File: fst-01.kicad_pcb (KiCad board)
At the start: 2 copper layers, 26.5 x 13.1 mm, 25 parts, among them J1 USB_A, K1 CONN_3, K2 CONN_2, K3 CONN_2, U1 STM32F103TB, U2 LP2985-33DBVR, U3 NUF2221W1, U4 SST25VF032B, X1 12MHz

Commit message: fst-01sz.
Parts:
- removed C10: 4.7uF, FST:c_0603
- removed C11: 0.1uF, FST:c_0402
- removed CE_mark: Symbol_CE_SilkScreen_5mm, Symbols:Symbol_CE_SilkScreen_5mm
- removed K2: CONN_2, SIL-2-0
- removed K3: CONN_2, SIL-2-2
- removed REF***: WEEE-Logo_4.2x6mm_SilkScreen, FST:WEEE-Logo_4.2x6mm_SilkScreen
- removed U4: SST25VF032B, WSON8
- added REF**: pad2, FST:pad1, F.Cu at (110.4, 93.6)
- added REF**: pad1, FST:pad1, F.Cu at (118.8, 94.2)
- C9: value 0.01uF -> 4.7uF; footprint FST:c_0402 -> FST:c_0603
- FST-LOGO: footprint FST-LOGO -> FST:FST-LOGO
- J1: footprint FST:USB-A-PLUG -> FST:USB-A-ZT01
- K1: footprint SIL-3-2 -> FST:SIL-5
- U2: value LP2985-33DBVR -> MCP1700-3302E; footprint FST:SOT23-5 -> Package_TO_SOT_SMD:SOT-23
- U3: footprint SOT363 -> FST:SOT363
- moved C2 15.0 mm to (123.5, 99.3), turned to 180 degrees
- moved X1 14.3 mm to (124.0, 101.9), turned to 90 degrees
- moved K1 13.4 mm to (112.8, 103.2)
- moved U3 11.9 mm to (112.8, 96.8), turned to 0 degrees
- moved D1 11.1 mm to (110.1, 99.0), turned to 270 degrees
- moved C1 11.0 mm to (121.8, 102.8), turned to 90 degrees
- moved C7 9.74 mm to (113.5, 100.8), turned to 90 degrees
- moved C8 9.69 mm to (121.6, 94.9), turned to 270 degrees
- moved C6 9.59 mm to (115.3, 94.5), turned to 0 degrees
- moved C4 8.92 mm to (121.8, 97.5), turned to 270 degrees
- moved C5 8.86 mm to (120.0, 102.5), turned to 180 degrees
- moved FST-LOGO 7.71 mm to (117.6, 98.6)
- moved R1 7.16 mm to (110.7, 101.5), turned to 180 degrees
- moved C3 6.86 mm to (117.7, 102.5), turned to 180 degrees
- moved C9 5.96 mm to (123.8, 94.2), turned to 0 degrees
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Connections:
- C9 pad 1: Net-(C9-Pad1) -> /VBUS
- D1 pad 1: GND -> Net-(D1-Pad1)
- D1 pad 2: Net-(D1-Pad2) -> /LED
- K1 pad 1: GND -> +3V3
- K1 pad 2: /SWCLK -> /SWDIO
- K1 pad 3: /SWDIO -> /SWCLK
- R1 pad 1: Net-(D1-Pad2) -> Net-(D1-Pad1)
- R1 pad 2: /LED -> GND
- U1 pad 10: /PA3 -> Net-(U1-Pad10)
- U1 pad 11: /NSS -> Net-(U1-Pad11)
- U1 pad 12: /CLK -> Net-(U1-Pad12)
- U1 pad 13: /MISO -> Net-(U1-Pad13)
- U1 pad 14: /MOSI -> Net-(U1-Pad14)
- U1 pad 15: /LED -> Net-(U1-Pad15)
- U1 pad 16: (no net) -> Net-(U1-Pad16)
- U1 pad 20: (no net) -> /LED
- U1 pad 21: (no net) -> Net-(U1-Pad21)
- U1 pad 22: (no net) -> Net-(U1-Pad22)
- U1 pad 29: (no net) -> Net-(U1-Pad29)
- U1 pad 30: (no net) -> Net-(U1-Pad30)
- U1 pad 31: (no net) -> Net-(U1-Pad31)
- U1 pad 32: (no net) -> Net-(U1-Pad32)
- U1 pad 33: (no net) -> Net-(U1-Pad33)
- U1 pad 34: (no net) -> Net-(U1-Pad34)
- U1 pad 7: (no net) -> Net-(U1-Pad7)
- U1 pad 8: (no net) -> Net-(U1-Pad8)
- U1 pad 9: /PA2 -> Net-(U1-Pad9)
- U2 pad 1: /VBUS -> GND
- U2 pad 2: GND -> +3V3
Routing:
- net +3V3: track 87.6 -> 53.1 mm, vias 6 -> 3
- net GND: track 94.2 -> 68.8 mm, vias 6 -> 2
- net /D-_PLUG: track 1.78 -> 18.2 mm, vias 0 -> 2
- net /MISO: track 12.7 -> 0.00 mm
- net /D+_PLUG: track 5.87 -> 17.8 mm, vias 0 -> 2
- net /NSS: track 10.5 -> 0.00 mm
- net /PA2: track 10.4 -> 0.00 mm
- net /NRST: track 2.17 -> 12.4 mm, vias 0 -> 2
- net /PA3: track 7.92 -> 0.00 mm
- net /MOSI: track 7.49 -> 0.00 mm
- net /VBUS: track 13.7 -> 6.37 mm
- net /CLK: track 5.52 -> 0.00 mm
- net Net-(U1-Pad10): track 0.00 -> 1.95 mm
- net /OSC_OUT: track 7.98 -> 6.38 mm
- net Net-(D1-Pad1): track 0.00 -> 1.41 mm
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- removed copper zone on F.Cu, net /VBUS
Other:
- board size 26.5 x 13.1 mm -> 20.8 x 12.2 mm
- rule pad_to_mask_clearance: 0.1524 -> 0.0762
- board text added: "FST-01SZ"
- board text removed: "FST-01G"

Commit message: More change.
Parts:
- removed the C4 at (121.8, 97.5)
- added C1: 0.1uF, FST:c_0402, F.Cu at (122.5, 97.5)
- moved C7 6.74 mm to (116.0, 94.5), turned to 0 degrees
- moved C6 6.33 mm to (114.3, 100.8), turned to 90 degrees
- moved C2 0.76 mm to (124.3, 99.3)
- moved C3 0.76 mm to (122.6, 102.8)
- moved C4 0.76 mm to (120.8, 102.5)
- moved C5 0.76 mm to (118.4, 102.5)
- moved C8 0.76 mm to (122.4, 94.9)
- moved C9 0.76 mm to (124.6, 94.2)
- moved K1 0.76 mm to (113.5, 103.2)
- moved REF** 0.76 mm to (119.6, 94.2)
- moved U1 0.76 mm to (118.3, 98.5)
- moved U2 0.76 mm to (125.1, 96.6)
- moved U3 0.76 mm to (113.6, 96.8)
- moved X1 0.76 mm to (124.8, 101.9)
- moved FST-LOGO 0.74 mm to (118.3, 98.7)
- renumbered C1 to C3, C5 to C4, C3 to C5
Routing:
- net GND: track 68.8 -> 77.4 mm
- net /VBUS: track 6.37 -> 4.36 mm
- net /D-_PLUG: track 18.2 -> 17.1 mm
- net /LED: track 5.85 -> 6.59 mm
- net +3V3: track 53.1 -> 52.5 mm
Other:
- board size 20.8 x 12.2 mm -> 21 x 12.6 mm
- net class Default: via_dia 0.8001 -> 0.8; via_drill 0.59944 -> 0.5
- net class GND: via_dia 0.8001 -> 0.8; via_drill 0.59944 -> 0.5
- net class VBUS: via_dia 0.8001 -> 0.8; via_drill 0.59944 -> 0.5
- net class VDD: via_dia 0.8001 -> 0.8; via_drill 0.59944 -> 0.5
- rule trace_min: 0.20066 -> 0.2
- rule via_min_drill: 0.50038 -> 0.5
- rule via_min_size: 0.8001 -> 0.8

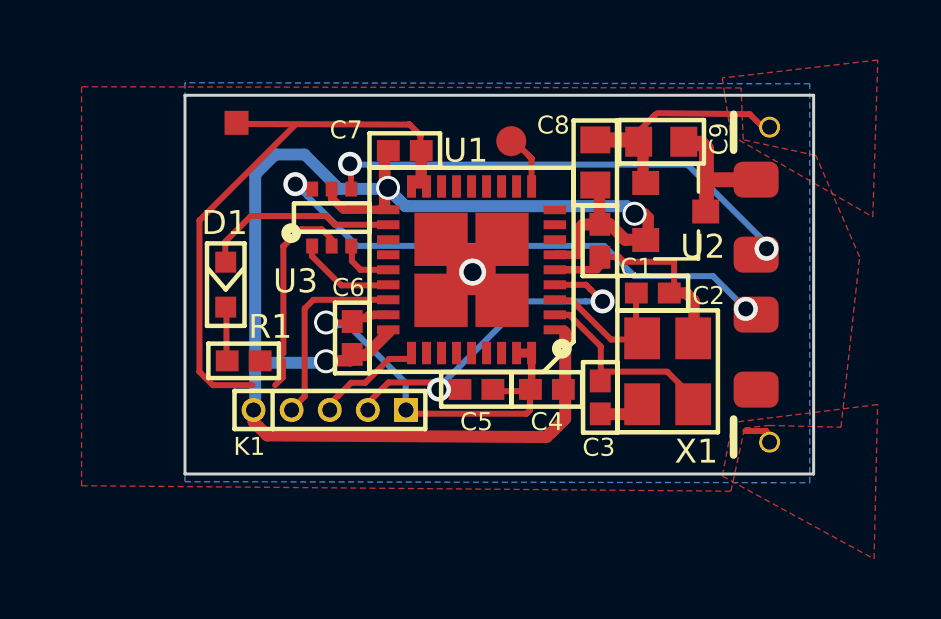
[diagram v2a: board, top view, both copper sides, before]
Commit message: Add hole sensor, drv5032.
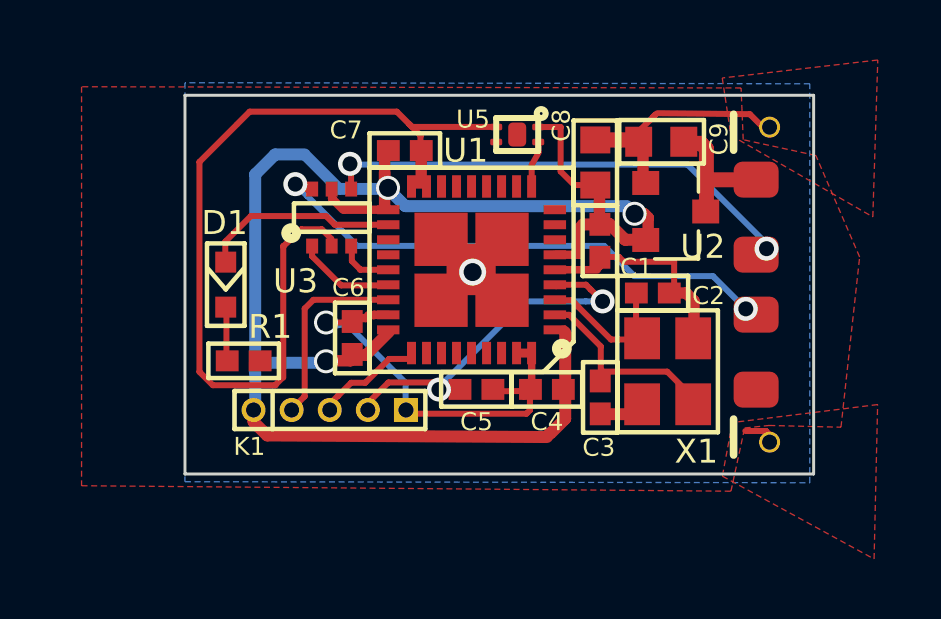
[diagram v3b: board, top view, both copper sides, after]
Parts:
- removed REF**: pad2, FST:pad1
- removed REF**: pad1, FST:pad1
- added U5: X2SON, FST:X2SON, F.Cu at (119.8, 94.0)
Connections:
- U1 pad 10: Net-(U1-Pad10) -> /PA3
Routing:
- net +3V3: track 52.5 -> 56.1 mm
- net GND: track 77.4 -> 80.8 mm
- net Net-(U1-Pad10): track 1.95 -> 0.00 mm
- net /PA3: track 0.00 -> 1.49 mm
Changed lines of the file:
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@@
     (thickness 1.6002)
     (drawings 6)
-    (tracks 258)
+    (tracks 263)
     (zones 0)
-    (modules 20)
+    (modules 19)
     (nets 33)
   )
@@
     (mod_text_size 1.524 1.524)
     (mod_text_width 0.3048)
-    (pad_size 1 1)
+    (pad_size 0.22 0.4)
     (pad_drill 0)
     (pad_to_mask_clearance 0.0762)
@@
   (net 30 "Net-(D1-Pad1)")
   (net 31 "Net-(U1-Pad14)")
-  (net 32 "Net-(U1-Pad10)")
+  (net 32 /PA3)
   (net_class Default "This is the default net class."
     (clearance 0.20066)
@@
     (add_net /OSC_IN)
     (add_net /OSC_OUT)
+    (add_net /PA3)
     (add_net /SWCLK)
     (add_net /SWDIO)
     (add_net /VBUS)
     (add_net "Net-(D1-Pad1)")
-    (add_net "Net-(U1-Pad10)")
     (add_net "Net-(U1-Pad11)")
     (add_net "Net-(U1-Pad12)")
@@
     (uvia_dia 0.50038)
     (uvia_drill 0.14986)
+  )
+  (module FST:X2SON (layer Front)
+    (at 119.7864 93.9927 270)
+    (fp_text reference U5 (at -0.508 1.4732 180) (layer F.SilkS)
+      (effects (font (size 0.6 0.6) (thickness 0.15)))
+    )
+    (fp_text value X2SON (at 0 -4.6 270) (layer F.Fab)
+      (effects (font (size 1 1) (thickness 0.15)))
+    )
+    (fp_circle (center -0.7 -0.8) (end -0.7 -0.7) (layer F.SilkS) (width 0.3))
+    (fp_line (start -0.55 -0.7) (end 0.55 -0.7) (layer F.SilkS) (width 0.2))
+    (fp_line (start 0.55 -0.7) (end 0.55 0.7) (layer F.SilkS) (width 0.2))
+    (fp_line (start 0.55 0.7) (end -0.55 0.7) (layer F.SilkS) (width 0.2))
+    (fp_line (start -0.55 0.7) (end -0.55 -0.7) (layer F.SilkS) (width 0.2))
+    (pad 5 smd roundrect (at 0 0 270) (size 0.8 0.6) (layers Front F.Paste F.Mask) (roundrect_rratio 0.25)
+      (solder_mask_margin 0.05) (clearance 0.05))
+    (pad 1 smd roundrect (at -0.25 -0.7 270) (size 0.22 0.4) (layers Front F.Paste F.Mask) (roundrect_rratio 0.25)
+      (net 13 +3V3) (solder_mask_margin 0.05) (clearance 0.05))
+    (pad 4 smd roundrect (at 0.25 -0.7 270) (size 0.22 0.4) (layers Front F.Paste F.Mask) (roundrect_rratio 0.25)
+      (net 32 /PA3) (solder_mask_margin 0.05) (clearance 0.05))
+    (pad 2 smd roundrect (at -0.25 0.7 270) (size 0.22 0.4) (layers Front F.Paste F.Mask) (roundrect_rratio 0.25)
+      (net 12 GND) (solder_mask_margin 0.05) (clearance 0.05))
+    (pad 3 smd roundrect (at 0.25 0.7 270) (size 0.22 0.4) (layers Front F.Paste F.Mask) (roundrect_rratio 0.25)
+      (solder_mask_margin 0.05) (clearance 0.05))
   )
   (module FST:QFN36 (layer Front)
@@
       (net 25 "Net-(U1-Pad11)") (solder_mask_margin 0.11))
     (pad 10 smd rect (at -2.00152 2.77622 180) (size 0.29972 0.7493) (layers Front F.Paste F.Mask)
-      (net 32 "Net-(U1-Pad10)") (solder_mask_margin 0.11))
+      (net 32 /PA3) (solder_mask_margin 0.11))
     (pad 9 smd rect (at -2.77622 2.00152 270) (size 0.29972 0.7493) (layers Front F.Paste F.Mask)
       (net 28 "Net-(U1-Pad9)") (solder_mask_margin 0.11))
@@
     )
   )
-  (module FST:pad1 (layer Front)
-    (at 110.43158 93.60408)
-    (fp_text reference REF** (at 0 1.57) (layer F.SilkS) hide
-      (effects (font (size 1 1) (thickness 0.15)))
-    )
-    (fp_text value pad2 (at -0.01 -1.53) (layer F.Fab)
-      (effects (font (size 1 1) (thickness 0.15)))
-    )
-    (pad 1 smd rect (at 0 0) (size 0.8 0.8) (layers Front F.Paste F.Mask)
-      (net 12 GND))
-  )
   (module FST:r_0402 (layer Front)
     (at 110.6678 101.5365 180)
@@
     (descr "SMT capacitor, 0603")
     (attr smd)
-    (fp_text reference C8 (at -1.24206 1.40208 180) (layer F.SilkS)
+    (fp_text reference C8 (at -1.23698 1.1303 270) (layer F.SilkS)
       (effects (font (size 0.59944 0.59944) (thickness 0.14986)))
     )
@@
     (pad 1 smd rect (at 0.75184 0 270) (size 0.89916 1.00076) (layers Front F.Paste F.Mask)
       (net 13 +3V3))
-  )
-  (module FST:pad1 (layer Front)
-    (at 119.58828 94.21368)
-    (fp_text reference REF** (at 0 1.57) (layer F.SilkS) hide
-      (effects (font (size 1 1) (thickness 0.15)))
-    )
-    (fp_text value pad1 (at -0.01 -1.53) (layer F.Fab)
-      (effects (font (size 1 1) (thickness 0.15)))
-    )
-    (pad 1 smd circle (at 0 0) (size 1 1) (layers Front F.Paste F.Mask)
-      (net 32 "Net-(U1-Pad10)"))
   )
   (gr_text FST-01SZ (at 123.4694 102.22738) (layer B.SilkS)
@@
   (segment (start 122.45594 98.50374) (end 122.555 98.40468) (width 0.20066) (layer Front) (net 12))
   (segment (start 115.488368 100.002211) (end 115.013718 100.002211) (width 0.2794) (layer Front) (net 12))
-  (segment (start 111.9632 101.3079) (end 111.99114 101.27996) (width 0.202) (layer Front) (net 12))
-  (segment (start 111.99114 101.27996) (end 111.99114 97.71126) (width 0.202) (layer Front) (net 12))
   (segment (start 113.27384 97.15246) (end 113.5888 97.46742) (width 0.202) (layer Front) (net 12))
   (segment (start 113.5888 97.46742) (end 113.5888 97.6884) (width 0.202) (layer Front) (net 12))
@@
   (segment (start 116.5733 94.0308) (end 116.18214 93.63964) (width 0.202) (layer Front) (net 12))
   (segment (start 111.97844 102.08641) (end 111.71809 102.34676) (width 0.20066) (layer Front) (net 12))
-  (segment (start 111.97844 101.5365) (end 111.97844 102.08641) (width 0.20066) (layer Front) (net 12))
   (segment (start 128.2 103.9965) (end 128.07934 103.87584) (width 0.20066) (layer Front) (net 12))
   (segment (start 128.07934 103.87584) (end 127.39116 103.87584) (width 0.20066) (layer Front) (net 12))
@@
   (segment (start 115.0239 100.00234) (end 115.01387 100.01237) (width 0.2794) (layer Front) (net 12))
   (segment (start 115.01387 100.01237) (end 114.841429 100.01237) (width 0.2794) (layer Front) (net 12))
-  (segment (start 110.45952 93.63964) (end 110.44936 93.6498) (width 0.202) (layer Front) (net 12))
-  (segment (start 116.205 93.6625) (end 110.45952 93.63964) (width 0.202) (layer Front) (net 12))
-  (segment (start 110.95609 102.34676) (end 109.638336 102.34676) (width 0.20066) (layer Front) (net 12))
-  (segment (start 109.1946 96.85528) (end 112.395 93.6625) (width 0.20066) (layer Front) (net 12))
-  (segment (start 109.1946 101.903024) (end 109.1946 96.85528) (width 0.20066) (layer Front) (net 12))
-  (segment (start 109.638336 102.34676) (end 109.1946 101.903024) (width 0.20066) (layer Front) (net 12))
   (segment (start 127.54102 93.31452) (end 128.143 93.9165) (width 0.20066) (layer Front) (net 12))
   (segment (start 124.46 93.2815) (end 127.54102 93.31452) (width 0.20066) (layer Front) (net 12))
+  (segment (start 110.86846 93.2307) (end 110.44936 93.6498) (width 0.202) (layer Front) (net 12))
+  (segment (start 116.205 93.6625) (end 115.7732 93.2307) (width 0.202) (layer Front) (net 12))
+  (segment (start 115.7732 93.2307) (end 110.86846 93.2307) (width 0.202) (layer Front) (net 12))
+  (segment (start 111.9886 97.7138) (end 111.99114 97.71126) (width 0.202) (layer Front) (net 12))
+  (segment (start 111.9886 102.0953) (end 111.9886 97.7138) (width 0.202) (layer Front) (net 12))
+  (segment (start 109.1946 94.9071) (end 110.4392 93.6625) (width 0.20066) (layer Front) (net 12))
+  (segment (start 109.1946 101.903024) (end 109.1946 94.9071) (width 0.20066) (layer Front) (net 12))
+  (segment (start 111.7346 102.3493) (end 109.640876 102.3493) (width 0.20066) (layer Front) (net 12))
+  (segment (start 109.640876 102.3493) (end 109.1946 101.903024) (width 0.20066) (layer Front) (net 12))
+  (segment (start 116.2812 93.7387) (end 116.205 93.6625) (width 0.20066) (layer Front) (net 12))
+  (segment (start 119.0498 93.7387) (end 116.2812 93.7387) (width 0.20066) (layer Front) (net 12))
   (via (at 123.698 96.63424) (size 0.8) (drill 0.6) (layers Front Back) (net 13))
   (segment (start 115.3668 96.3422) (end 115.5192 96.4946) (width 0.2794) (layer Front) (net 13))
@@
   (segment (start 110.998 103.1875) (end 110.998 103.5685) (width 0.4) (layer Front) (net 13))
   (segment (start 110.998 103.5685) (end 111.45266 104.02316) (width 0.4) (layer Front) (net 13))
+  (segment (start 121.2342 93.7427) (end 120.4864 93.7427) (width 0.20066) (layer Front) (net 13))
+  (segment (start 122.3899 95.67672) (end 121.68886 95.67672) (width 0.20066) (layer Front) (net 13))
+  (segment (start 121.2342 95.22206) (end 121.2342 93.7427) (width 0.20066) (layer Front) (net 13))
+  (segment (start 121.68886 95.67672) (end 121.2342 95.22206) (width 0.20066) (layer Front) (net 13))
   (segment (start 110.09376 101.31044) (end 110.09376 99.90074) (width 0.20066) (layer Front) (net 30) (status 30))
-  (segment (start 120.25884 95.141569) (end 120.26646 95.149189) (width 0.20066) (layer Front) (net 32))
-  (segment (start 120.266108 94.789908) (end 120.16232 94.68612) (width 0.20066) (layer Front) (net 32))
-  (segment (start 120.266108 95.724851) (end 120.266108 94.789908) (width 0.20066) (layer Front) (net 32))
-  (segment (start 120.25884 94.78264) (end 119.65432 94.17812) (width 0.20066) (layer Front) (net 32))
-  (segment (start 120.25884 94.78518) (end 120.25884 94.78264) (width 0.20066) (layer Front) (net 32))
+  (segment (start 120.4976 94.5769) (end 120.4976 94.2721) (width 0.20066) (layer Front) (net 32))
+  (segment (start 120.269 95.0087) (end 120.4976 94.6023) (width 0.20066) (layer Front) (net 32))
+  (segment (start 120.266108 95.724851) (end 120.269 95.721959) (width 0.20066) (layer Front) (net 32))
+  (segment (start 120.269 95.721959) (end 120.269 95.0087) (width 0.20066) (layer Front) (net 32))
   (zone (net 12) (net_name GND) (layer Front) (hatch none 0.508)
     (connect_pads (clearance 0.254))

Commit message: More change to PCBA.
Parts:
- moved U4 10.7 mm to (109.9, 97.9), turned to 0 degrees
- moved D1 1.66 mm to (109.9, 100.7)
- moved R1 0.87 mm to (111.2, 100.8), turned to 270 degrees
- moved U3 0.60 mm to (113.0, 96.8)
- moved C8 0.36 mm to (122.8, 94.9)
- moved C7 0.33 mm to (116.0, 94.2)
- moved C9 0.31 mm to (124.9, 94.2)
- moved C5 0.29 mm to (118.3, 102.8)
- moved C6 0.29 mm to (114.0, 100.8)
- moved C4 0.27 mm to (120.7, 102.8)
- moved X1 0.11 mm to (124.8, 102.0)
- moved C3 0.11 mm to (122.5, 102.8)
- moved C1 0.06 mm to (122.6, 97.5)
- renumbered U5 to U4
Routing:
- net +3V3: track 56.1 -> 77.0 mm, vias 3 -> 4
- net /PA3: track 1.49 -> 14.7 mm, vias 0 -> 2
- net GND: track 80.8 -> 73.3 mm
- net /LED: track 6.59 -> 8.28 mm
- net /D+_PLUG: track 17.4 -> 18.1 mm
- net /D+: track 3.30 -> 3.94 mm
- net /VBUS: track 4.36 -> 3.80 mm
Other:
- board size 21 x 12.6 mm -> 21.2 x 12.6 mm
